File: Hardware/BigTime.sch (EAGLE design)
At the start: 13 parts, among them U1 ATMEGA328P_PDIP_EZ, Y1 32.768kHz

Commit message: Mods for threaded inserts, PTH battery holder. - Modified .sch and .brd files to V13 to add PTH battery holder. - Modified enclosure file to change thickness of layer 1 and hole    sizes on layer 1 to 3.9mm.
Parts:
- BAT: value BATTERY-COIN-CELL-W-THERMALSW-THERMALS -> (none); device Testing:BATTERY-COIN-CELL-W-THERMALSW-THERMALS -> SparkFun-Electromechanical:BATTERYFOB
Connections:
- net GND: now also BAT.-; no longer BAT1.-
- net VCC: now also BAT.+; no longer BAT1.+, BATG$2.P$1, BATG$3.P$1, BATG$4.P$1
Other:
- note added: "Changes to v14 (2/13/13 MAH):"
- note added: "V14"
- note added: "change coin cell to PTH"

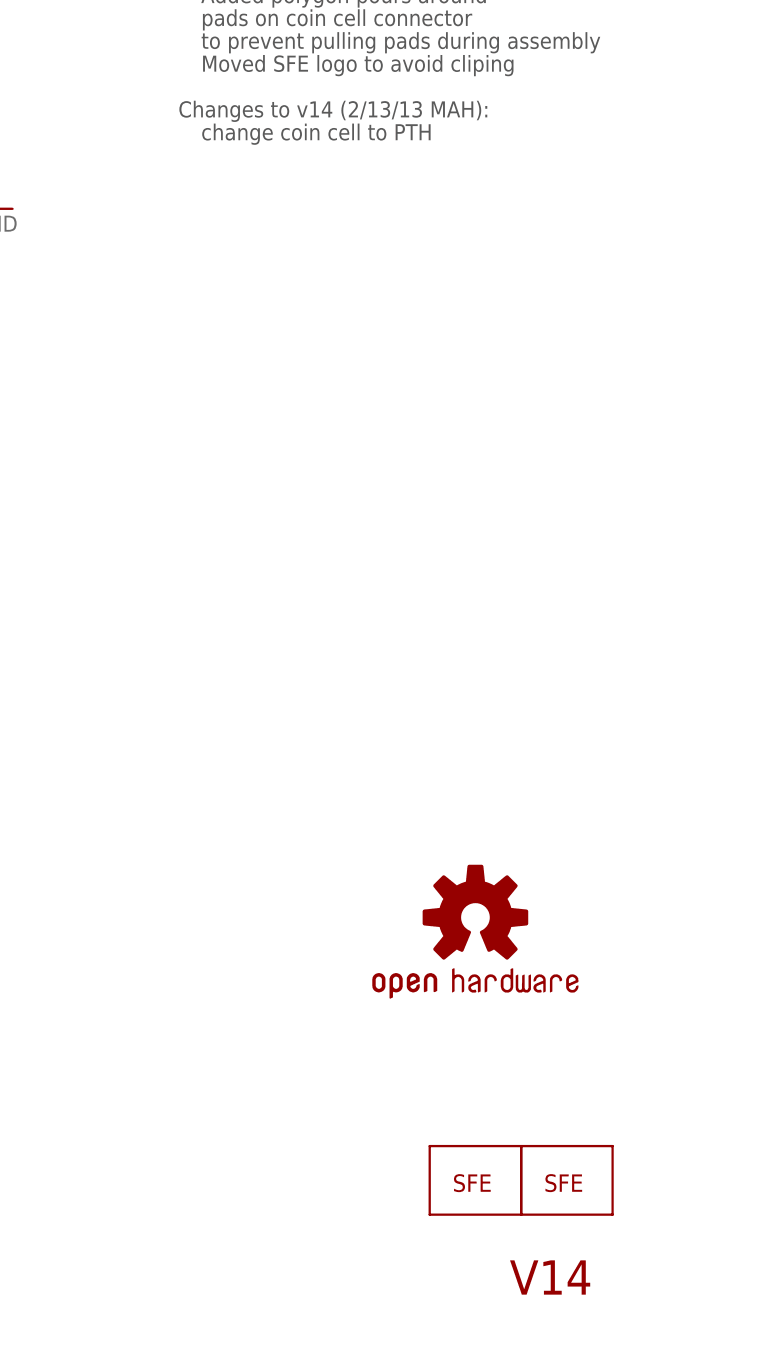
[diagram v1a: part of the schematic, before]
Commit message: Tweaks to board, enclosure, repo - Enclosure:  * Hole size in layer 1 is now right for threaded inserts  * Change thickness note on layers 2 and 3 to 1/8"  * Moved lever from center of layer 3 to ensure thickness of plastic would be the same - Board:  * Tweak battery holder down slightly, as it was interfering with display  * Change to rev 15 - Repo: move enclosure file to top level, per SparkFun standards
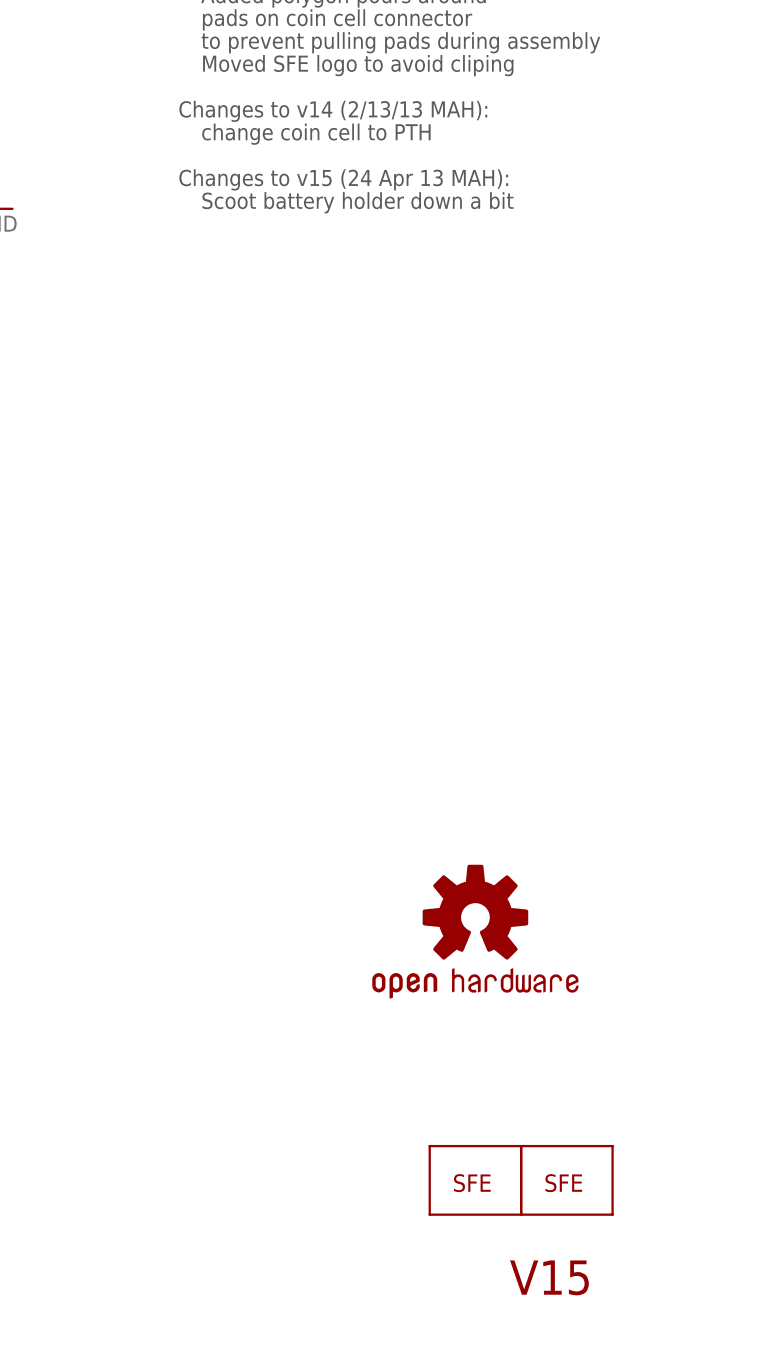
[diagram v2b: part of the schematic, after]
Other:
- note added: "Changes to v15 (24 Apr 13 MAH):"
- note added: "Scoot battery holder down a bit"
- note added: "V15"
- note removed: "V14"
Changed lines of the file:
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@@
 <?xml version="1.0" encoding="utf-8"?>
 <!DOCTYPE eagle SYSTEM "eagle.dtd">
-<eagle version="6.3">
+<eagle version="6.4">
 <drawing>
 <settings>
@@
 <grid distance="0.1" unitdist="inch" unit="inch" style="lines" multiple="1" display="no" altdistance="0.01" altunitdist="inch" altunit="inch"/>
 <layers>
-<layer number="1" name="Top" color="4" fill="1" visible="yes" active="no"/>
-<layer number="2" name="Route2" color="1" fill="3" visible="yes" active="no"/>
-<layer number="3" name="Route3" color="4" fill="3" visible="yes" active="no"/>
-<layer number="4" name="Route4" color="1" fill="4" visible="yes" active="no"/>
-<layer number="5" name="Route5" color="4" fill="4" visible="yes" active="no"/>
-<layer number="6" name="Route6" color="1" fill="8" visible="yes" active="no"/>
-<layer number="7" name="Route7" color="4" fill="8" visible="yes" active="no"/>
-<layer number="8" name="Route8" color="1" fill="2" visible="yes" active="no"/>
-<layer number="9" name="Route9" color="4" fill="2" visible="yes" active="no"/>
-<layer number="10" name="Route10" color="1" fill="7" visible="yes" active="no"/>
-<layer number="11" name="Route11" color="4" fill="7" visible="yes" active="no"/>
-<layer number="12" name="Route12" color="1" fill="5" visible="yes" active="no"/>
-<layer number="13" name="Route13" color="4" fill="5" visible="yes" active="no"/>
-<layer number="14" name="Route14" color="1" fill="6" visible="yes" active="no"/>
-<layer number="15" name="Route15" color="4" fill="6" visible="yes" active="no"/>
-<layer number="16" name="Bottom" color="1" fill="1" visible="yes" active="no"/>
-<layer number="17" name="Pads" color="2" fill="1" visible="yes" active="no"/>
-<layer number="18" name="Vias" color="2" fill="1" visible="yes" active="no"/>
-<layer number="19" name="Unrouted" color="14" fill="1" visible="yes" active="no"/>
-<layer number="20" name="Dimension" color="15" fill="1" visible="yes" active="no"/>
-<layer number="21" name="tPlace" color="16" fill="1" visible="yes" active="no"/>
-<layer number="22" name="bPlace" color="14" fill="1" visible="yes" active="no"/>
-<layer number="23" name="tOrigins" color="15" fill="1" visible="yes" active="no"/>
-<layer number="24" name="bOrigins" color="15" fill="1" visible="yes" active="no"/>
-<layer number="25" name="tNames" color="7" fill="1" visible="yes" active="no"/>
-<layer number="26" name="bNames" color="7" fill="1" visible="yes" active="no"/>
-<layer number="27" name="tValues" color="7" fill="1" visible="yes" active="no"/>
-<layer number="28" name="bValues" color="7" fill="1" visible="yes" active="no"/>
+<layer number="1" name="Top" color="4" fill="1" visible="no" active="no"/>
+<layer number="2" name="Route2" color="1" fill="3" visible="no" active="no"/>
+<layer number="3" name="Route3" color="4" fill="3" visible="no" active="no"/>
+<layer number="4" name="Route4" color="1" fill="4" visible="no" active="no"/>
+<layer number="5" name="Route5" color="4" fill="4" visible="no" active="no"/>
+<layer number="6" name="Route6" color="1" fill="8" visible="no" active="no"/>
+<layer number="7" name="Route7" color="4" fill="8" visible="no" active="no"/>
+<layer number="8" name="Route8" color="1" fill="2" visible="no" active="no"/>
+<layer number="9" name="Route9" color="4" fill="2" visible="no" active="no"/>
+<layer number="10" name="Route10" color="1" fill="7" visible="no" active="no"/>
+<layer number="11" name="Route11" color="4" fill="7" visible="no" active="no"/>
+<layer number="12" name="Route12" color="1" fill="5" visible="no" active="no"/>
+<layer number="13" name="Route13" color="4" fill="5" visible="no" active="no"/>
+<layer number="14" name="Route14" color="1" fill="6" visible="no" active="no"/>
+<layer number="15" name="Route15" color="4" fill="6" visible="no" active="no"/>
+<layer number="16" name="Bottom" color="1" fill="1" visible="no" active="no"/>
+<layer number="17" name="Pads" color="2" fill="1" visible="no" active="no"/>
+<layer number="18" name="Vias" color="2" fill="1" visible="no" active="no"/>
+<layer number="19" name="Unrouted" color="14" fill="1" visible="no" active="no"/>
+<layer number="20" name="Dimension" color="15" fill="1" visible="no" active="no"/>
+<layer number="21" name="tPlace" color="16" fill="1" visible="no" active="no"/>
+<layer number="22" name="bPlace" color="14" fill="1" visible="no" active="no"/>
+<layer number="23" name="tOrigins" color="15" fill="1" visible="no" active="no"/>
+<layer number="24" name="bOrigins" color="15" fill="1" visible="no" active="no"/>
+<layer number="25" name="tNames" color="7" fill="1" visible="no" active="no"/>
+<layer number="26" name="bNames" color="7" fill="1" visible="no" active="no"/>
+<layer number="27" name="tValues" color="7" fill="1" visible="no" active="no"/>
+<layer number="28" name="bValues" color="7" fill="1" visible="no" active="no"/>
 <layer number="29" name="tStop" color="7" fill="3" visible="no" active="no"/>
 <layer number="30" name="bStop" color="7" fill="6" visible="no" active="no"/>
@@
 <layer number="35" name="tGlue" color="7" fill="4" visible="no" active="no"/>
 <layer number="36" name="bGlue" color="7" fill="5" visible="no" active="no"/>
-<layer number="37" name="tTest" color="7" fill="1" visible="yes" active="no"/>
-<layer number="38" name="bTest" color="7" fill="1" visible="yes" active="no"/>
+<layer number="37" name="tTest" color="7" fill="1" visible="no" active="no"/>
+<layer number="38" name="bTest" color="7" fill="1" visible="no" active="no"/>
 <layer number="39" name="tKeepout" color="4" fill="11" visible="no" active="no"/>
 <layer number="40" name="bKeepout" color="1" fill="11" visible="no" active="no"/>
@@
 <layer number="44" name="Drills" color="7" fill="1" visible="no" active="no"/>
 <layer number="45" name="Holes" color="7" fill="1" visible="no" active="no"/>
-<layer number="46" name="Milling" color="3" fill="1" visible="yes" active="no"/>
-<layer number="47" name="Measures" color="7" fill="1" visible="yes" active="no"/>
-<layer number="48" name="Document" color="7" fill="1" visible="yes" active="no"/>
-<layer number="49" name="Reference" color="7" fill="1" visible="yes" active="no"/>
-<layer number="50" name="dxf" color="7" fill="1" visible="yes" active="no"/>
-<layer number="51" name="tDocu" color="6" fill="1" visible="yes" active="no"/>
-<layer number="52" name="bDocu" color="7" fill="1" visible="yes" active="no"/>
-<layer number="53" name="tGND_GNDA" color="7" fill="9" visible="yes" active="no"/>
-<layer number="54" name="bGND_GNDA" color="1" fill="9" visible="yes" active="no"/>
-<layer number="56" name="wert" color="7" fill="1" visible="yes" active="no"/>
+<layer number="46" name="Milling" color="3" fill="1" visible="no" active="no"/>
+<layer number="47" name="Measures" color="7" fill="1" visible="no" active="no"/>
+<layer number="48" name="Document" color="7" fill="1" visible="no" active="no"/>
+<layer number="49" name="Reference" color="7" fill="1" visible="no" active="no"/>
+<layer number="50" name="dxf" color="7" fill="1" visible="no" active="no"/>
+<layer number="51" name="tDocu" color="6" fill="1" visible="no" active="no"/>
+<layer number="52" name="bDocu" color="7" fill="1" visible="no" active="no"/>
+<layer number="53" name="tGND_GNDA" color="7" fill="9" visible="no" active="no"/>
+<layer number="54" name="bGND_GNDA" color="1" fill="9" visible="no" active="no"/>
+<layer number="56" name="wert" color="7" fill="1" visible="no" active="no"/>
 <layer number="91" name="Nets" color="2" fill="1" visible="yes" active="yes"/>
 <layer number="92" name="Busses" color="1" fill="1" visible="yes" active="yes"/>
@@
 <text x="200.66" y="137.16" size="1.778" layer="97">Changes to v14 (2/13/13 MAH):</text>
 <text x="203.2" y="134.62" size="1.778" layer="97">change coin cell to PTH</text>
-<text x="237.49" y="6.35" size="3.81" layer="94">V14</text>
+<text x="237.49" y="6.35" size="3.81" layer="94">V15</text>
+<text x="200.66" y="129.54" size="1.778" layer="97">Changes to v15 (24 Apr 13 MAH):</text>
+<text x="203.2" y="127" size="1.778" layer="97">Scoot battery holder down a bit</text>
 </plain>
 <instances>
